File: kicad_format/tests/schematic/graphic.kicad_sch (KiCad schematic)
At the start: 34 parts, among them P10 CONN_1, P11 CONN_1, P12 CONN_1, P4 CONN_2, P5 CONN_5, P9 CONN_1, U2 4C4001, U21 XC1736APD8, U23 XC4003/PQ100, U24 XC4005-PQ160, U7 AV9173, X1 10MHz

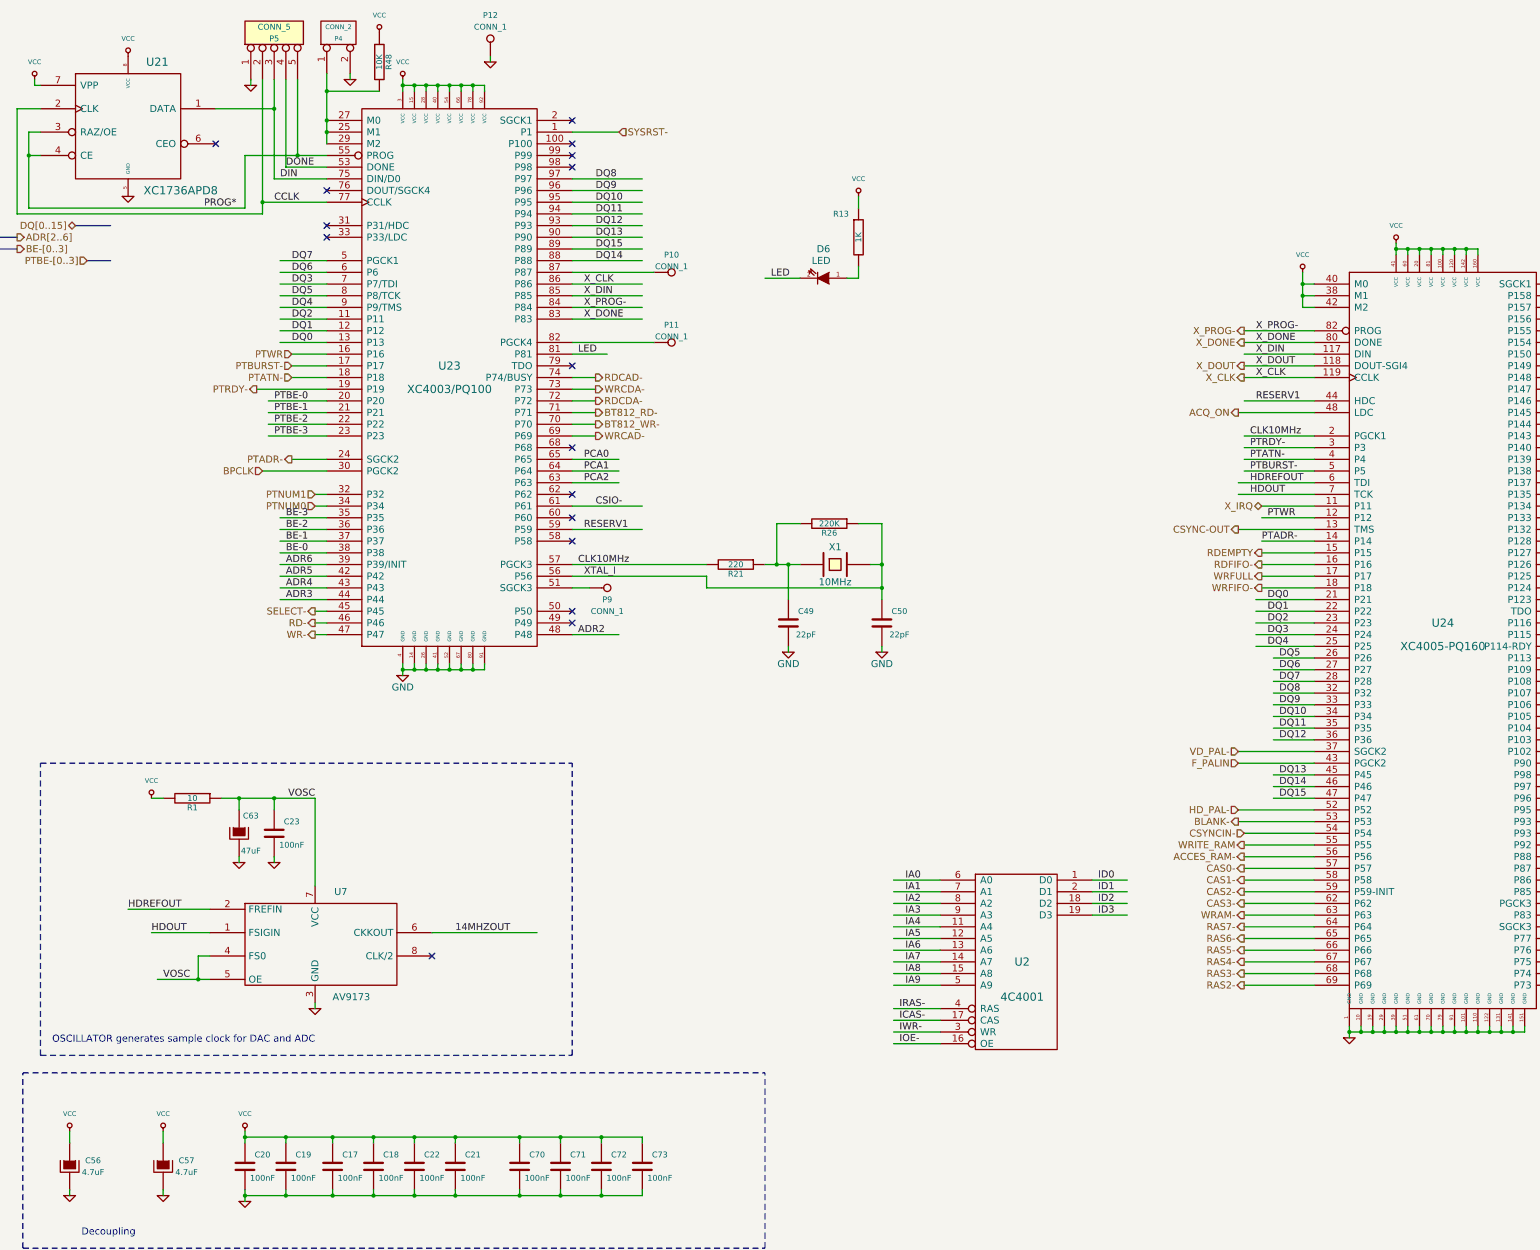
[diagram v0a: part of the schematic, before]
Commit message: Add serialization context and support most modern kicad file idiosyncrasies
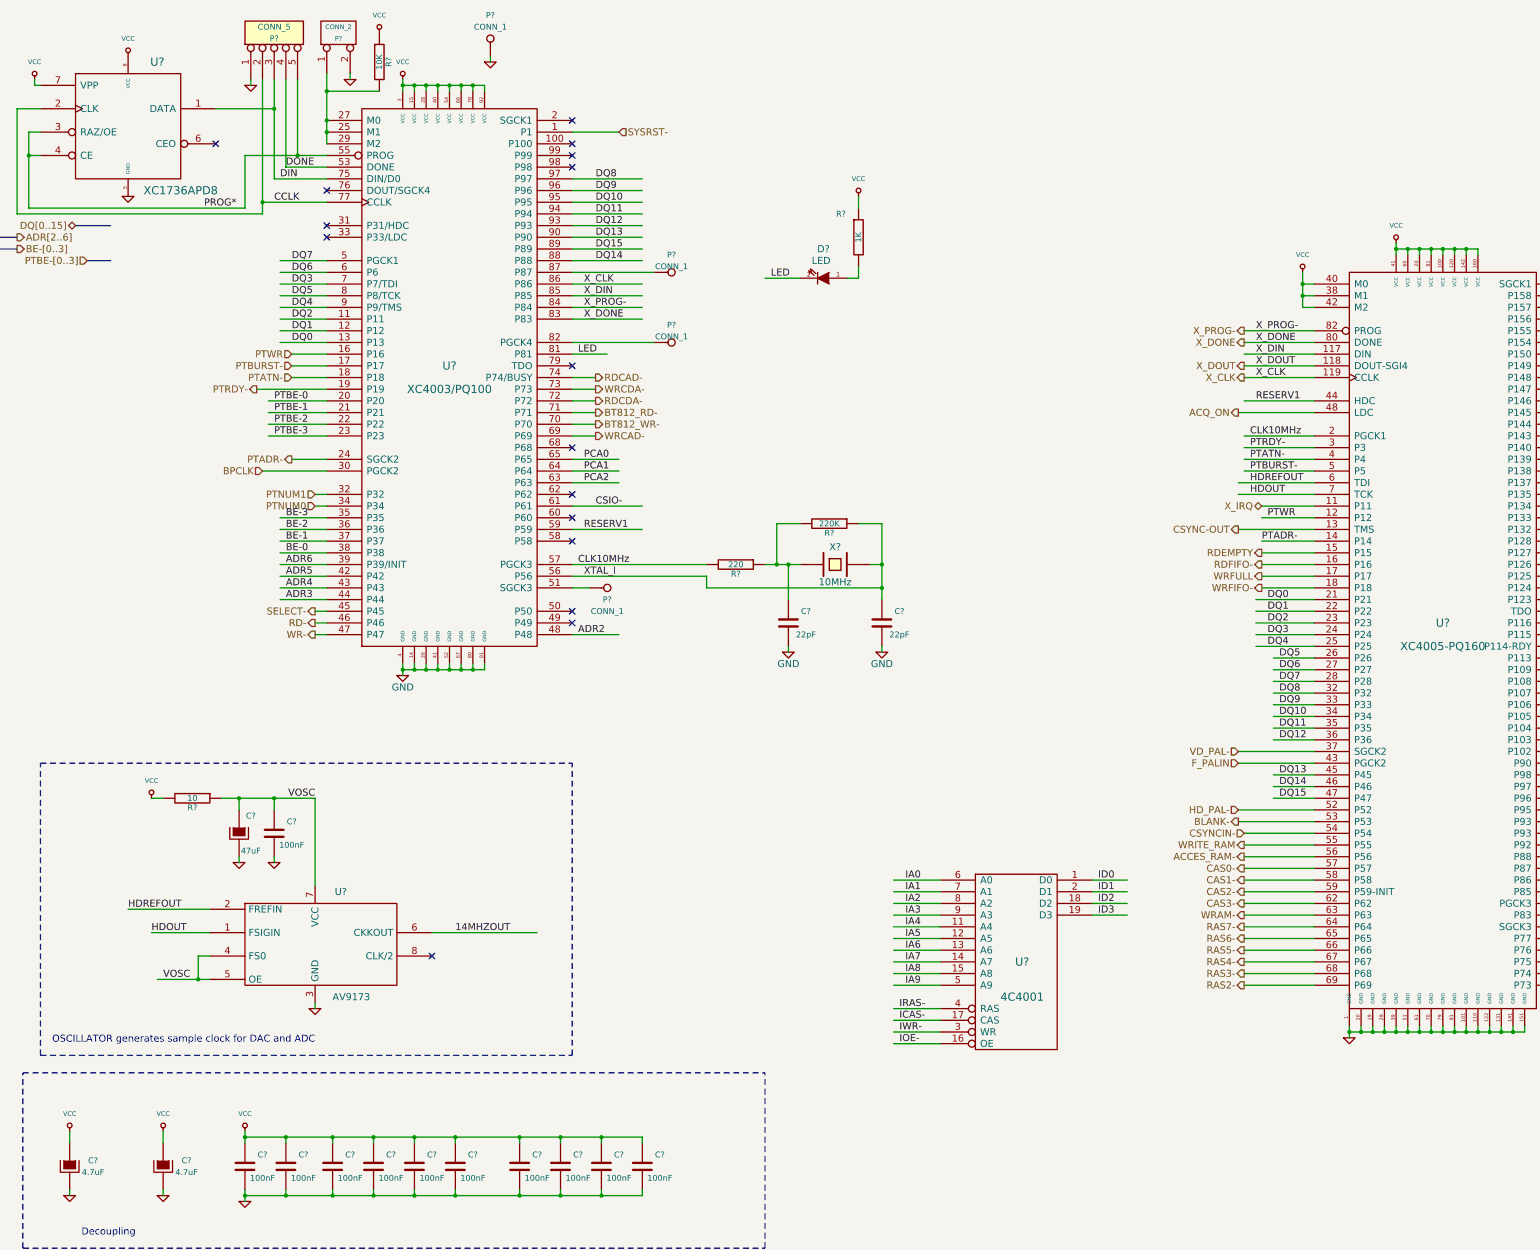
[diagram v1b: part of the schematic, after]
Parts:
- renumbered C63 to C?, C21 to C?, C22 to C?, C23 to C?, C70 to C?, C71 to C?, C72 to C?, C73 to C?, C18 to C?, C50 to C?, C56 to C?, C20 to C?, C57 to C?, C19 to C?, C17 to C?, C49 to C?, D6 to D?, P5 to P?, P4 to P?, P9 to P?, P12 to P?, P10 to P?, P11 to P?, R13 to R?, R1 to R?, R48 to R?, R21 to R?, R26 to R?, U7 to U?, U24 to U?, U21 to U?, U2 to U?, U23 to U?, X1 to X?
